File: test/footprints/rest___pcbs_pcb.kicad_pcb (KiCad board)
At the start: 2 copper layers, 2.4 x 14.2 mm, 10 parts, among them J1 Jumper

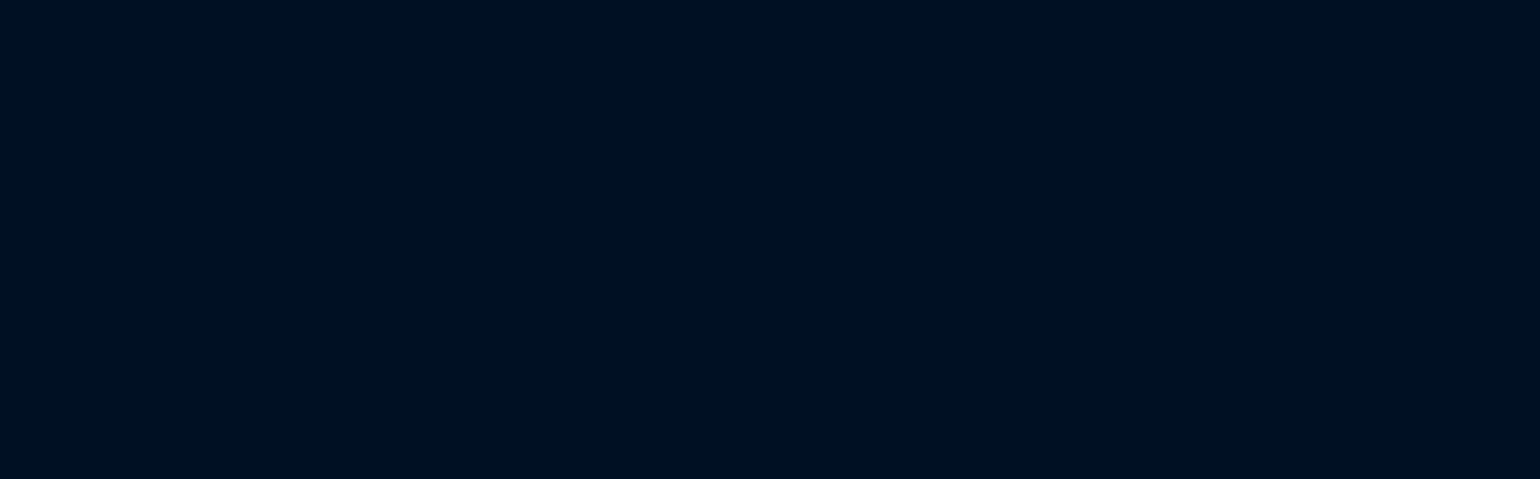
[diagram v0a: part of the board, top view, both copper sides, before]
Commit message: expand code coverage for rest of footprints
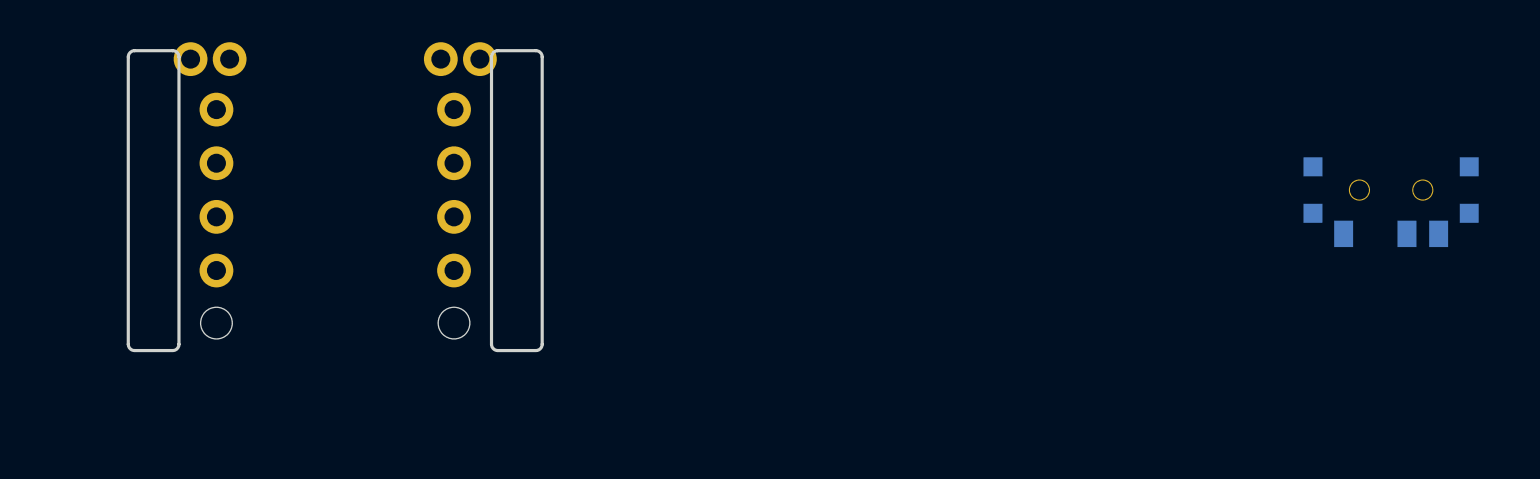
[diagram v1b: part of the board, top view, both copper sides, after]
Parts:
- added REF**: RollerEncoder_Panasonic_EVQWGD001, RollerEncoder_Panasonic_EVQWGD001, F.Cu at (50.0, -150.0)
- added T2: , E73:SPDT_C128955, F.Cu at (100.0, -150.0)
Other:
- board size 2.4 x 14.2 mm -> 19.6 x 14.2 mm
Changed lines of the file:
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@@
       (pad 1 thru_hole circle (at 0 0) (size 0.6 0.6) (drill 0.3) (layers *.Cu) (zone_connect 2) (net 15 "net"))
       )
+        (module RollerEncoder_Panasonic_EVQWGD001 (layer F.Cu)
+        (at 50 -150 0)
+        (fp_text reference REF** (at 0 0 0) (layer F.Fab) (effects (font (size 1 1) (thickness 0.15))))
+        (fp_text value RollerEncoder_Panasonic_EVQWGD001 (at -0.1 9 0) (layer F.Fab) (effects (font (size 1 1) (thickness 0.15))))
+        (fp_line (start -8.4 -6.4) (end 8.4 -6.4) (layer Dwgs.User) (width 0.12))
+        (fp_line (start 8.4 -6.4) (end 8.4 7.4) (layer Dwgs.User) (width 0.12))
+        (fp_line (start 8.4 7.4) (end -8.4 7.4) (layer Dwgs.User) (width 0.12))
+        (fp_line (start -8.4 7.4) (end -8.4 -6.4) (layer Dwgs.User) (width 0.12))
+          (fp_line (start 9.8 7.3) (end 9.8 -6.3) (layer Edge.Cuts) (width 0.15))
+          (fp_line (start 7.4 -6.3) (end 7.4 7.3) (layer Edge.Cuts) (width 0.15))
+          (fp_line (start 9.5 -6.6) (end 7.7 -6.6) (layer Edge.Cuts) (width 0.15))
+          (fp_line (start 7.7 7.6) (end 9.5 7.6) (layer Edge.Cuts) (width 0.15))
+          (fp_arc (start 7.7 7.3) (end 7.4 7.3) (angle -90) (layer Edge.Cuts) (width 0.15))
+          (fp_arc (start 9.5 7.3) (end 9.5 7.6) (angle -90) (layer Edge.Cuts) (width 0.15))
+          (fp_arc (start 7.7 -6.3) (end 7.7 -6.6) (angle -90) (layer Edge.Cuts) (width 0.15))
+          (fp_arc (start 9.5 -6.3) (end 9.8 -6.3) (angle -90) (layer Edge.Cuts) (width 0.15))
+          (pad S1 thru_hole circle (at -6.85 -6.2 0) (size 1.6 1.6) (drill 0.9) (layers *.Cu *.Mask) (net 1 "from"))
+          (pad S2 thru_hole circle (at -5 -6.2 0) (size 1.6 1.6) (drill 0.9) (layers *.Cu *.Mask) (net 2 "to"))
+          (pad A thru_hole circle (at -5.625 -3.81 0) (size 1.6 1.6) (drill 0.9) (layers *.Cu *.Mask) (net 11 "A"))
+          (pad B thru_hole circle (at -5.625 -1.27 0) (size 1.6 1.6) (drill 0.9) (layers *.Cu *.Mask) (net 12 "B"))
+          (pad C thru_hole circle (at -5.625 1.27 0) (size 1.6 1.6) (drill 0.9) (layers *.Cu *.Mask) (net 13 "C"))
+          (pad D thru_hole circle (at -5.625 3.81 0) (size 1.6 1.6) (drill 0.9) (layers *.Cu *.Mask) (net 14 "D"))
+          (pad "" np_thru_hole circle (at -5.625 6.3 0) (size 1.5 1.5) (drill 1.5) (layers *.Cu *.Mask))
+          (fp_line (start -9.8 7.3) (end -9.8 -6.3) (layer Edge.Cuts) (width 0.15))
+          (fp_line (start -7.4 -6.3) (end -7.4 7.3) (layer Edge.Cuts) (width 0.15))
+          (fp_line (start -9.5 -6.6) (end -7.7 -6.6) (layer Edge.Cuts) (width 0.15))
+          (fp_line (start -7.7 7.6) (end -9.5 7.6) (layer Edge.Cuts) (width 0.15))
+          (fp_arc (start -7.7 7.3) (end -7.4 7.3) (angle 90) (layer Edge.Cuts) (width 0.15))
+          (fp_arc (start -9.5 7.3) (end -9.5 7.6) (angle 90) (layer Edge.Cuts) (width 0.15))
+          (fp_arc (start -7.7 -6.3) (end -7.7 -6.6) (angle 90) (layer Edge.Cuts) (width 0.15))
+          (fp_arc (start -9.5 -6.3) (end -9.8 -6.3) (angle 90) (layer Edge.Cuts) (width 0.15))
+          (pad S1 thru_hole circle (at 6.85 -6.2 0) (size 1.6 1.6) (drill 0.9) (layers *.Cu *.Mask) (net 1 "from"))
+          (pad S2 thru_hole circle (at 5 -6.2 0) (size 1.6 1.6) (drill 0.9) (layers *.Cu *.Mask) (net 2 "to"))
+          (pad A thru_hole circle (at 5.625 -3.81 0) (size 1.6 1.6) (drill 0.9) (layers *.Cu *.Mask) (net 11 "A"))
+          (pad B thru_hole circle (at 5.625 -1.27 0) (size 1.6 1.6) (drill 0.9) (layers *.Cu *.Mask) (net 12 "B"))
+          (pad C thru_hole circle (at 5.625 1.27 0) (size 1.6 1.6) (drill 0.9) (layers *.Cu *.Mask) (net 13 "C"))
+          (pad D thru_hole circle (at 5.625 3.81 0) (size 1.6 1.6) (drill 0.9) (layers *.Cu *.Mask) (net 14 "D"))
+          (pad "" np_thru_hole circle (at 5.625 6.3 0) (size 1.5 1.5) (drill 1.5) (layers *.Cu *.Mask))
+        )
+        (module E73:SPDT_C128955 (layer F.Cu)
+            (at 100 -150 0)
+            (fp_text reference "T2" (at 0 0) (layer F.SilkS) hide (effects (font (size 1.27 1.27) (thickness 0.15))))
+            (fp_text value "" (at 0 0) (layer F.SilkS) hide (effects (font (size 1.27 1.27) (thickness 0.15))))
+            (fp_line (start 1.95 -1.35) (end -1.95 -1.35) (layer B.SilkS) (width 0.15))
+            (fp_line (start 0 -1.35) (end -3.3 -1.35) (layer B.SilkS) (width 0.15))
+            (fp_line (start -3.3 -1.35) (end -3.3 1.5) (layer B.SilkS) (width 0.15))
+            (fp_line (start -3.3 1.5) (end 3.3 1.5) (layer B.SilkS) (width 0.15))
+            (fp_line (start 3.3 1.5) (end 3.3 -1.35) (layer B.SilkS) (width 0.15))
+            (fp_line (start 0 -1.35) (end 3.3 -1.35) (layer B.SilkS) (width 0.15))
+            (fp_line (start -1.95 -3.85) (end 1.95 -3.85) (layer Dwgs.User) (width 0.15))
+            (fp_line (start 1.95 -3.85) (end 1.95 -1.35) (layer Dwgs.User) (width 0.15))
+            (fp_line (start -1.95 -1.35) (end -1.95 -3.85) (layer Dwgs.User) (width 0.15))
+            (pad "" np_thru_hole circle (at 1.5 0) (size 1 1) (drill 0.9) (layers *.Cu *.Mask))
+            (pad "" np_thru_hole circle (at -1.5 0) (size 1 1) (drill 0.9) (layers *.Cu *.Mask))
+            (pad 1 smd rect (at -2.25 2.075 0) (size 0.9 1.25) (layers B.Cu B.Paste B.Mask) (net 1 "from"))
+            (pad 2 smd rect (at 0.75 2.075 0) (size 0.9 1.25) (layers B.Cu B.Paste B.Mask) (net 2 "to"))
+            (pad 3 smd rect (at 2.25 2.075 0) (size 0.9 1.25) (layers B.Cu B.Paste B.Mask))
+            (pad "" smd rect (at 3.7 -1.1 0) (size 0.9 0.9) (layers B.Cu B.Paste B.Mask))
+            (pad "" smd rect (at 3.7 1.1 0) (size 0.9 0.9) (layers B.Cu B.Paste B.Mask))
+            (pad "" smd rect (at -3.7 1.1 0) (size 0.9 0.9) (layers B.Cu B.Paste B.Mask))
+            (pad "" smd rect (at -3.7 -1.1 0) (size 0.9 0.9) (layers B.Cu B.Paste B.Mask))
+        )
 )
